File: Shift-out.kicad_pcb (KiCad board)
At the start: 2 copper layers, 116.8 x 33 mm, 23 parts, among them P1 CONN_02X08, P10 CONN_01X08, P11 CONN_01X02, P2 CONN_01X08, P3 CONN_02X08, P4 CONN_01X08, P5 INPUT, P6 CONN_02X08, P7 EXPANSION, P8 CONN_01X08, P9 CONN_02X08, U1 74HC595, U2 74HC595, U3 74HC595, U4 74HC595

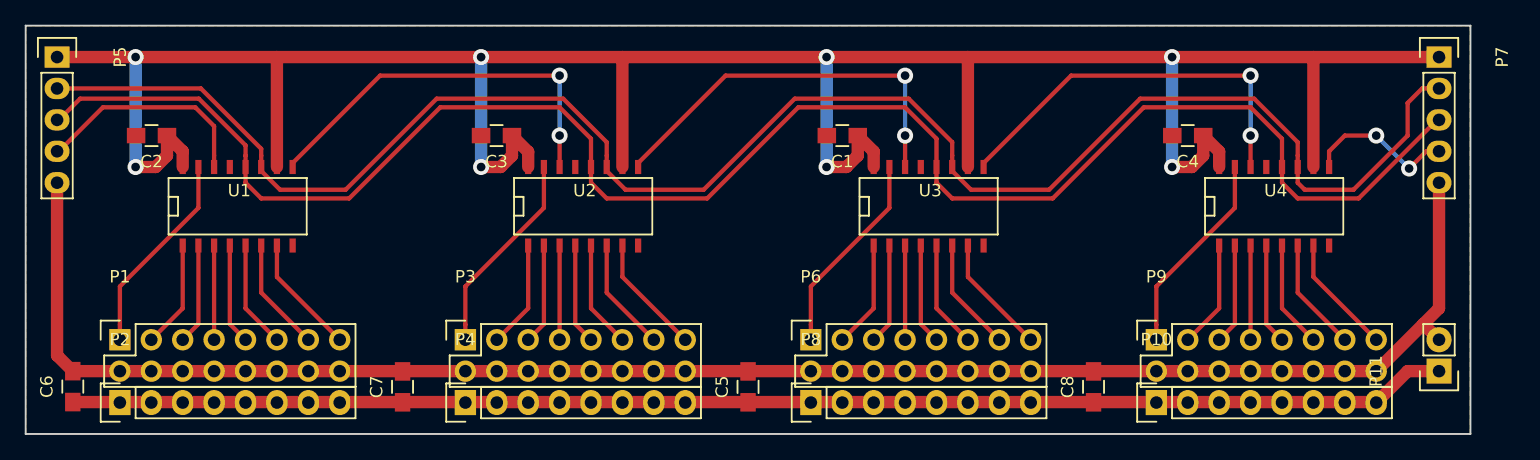
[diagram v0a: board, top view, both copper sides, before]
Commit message: Modified output connector to allow direct servo plugging.
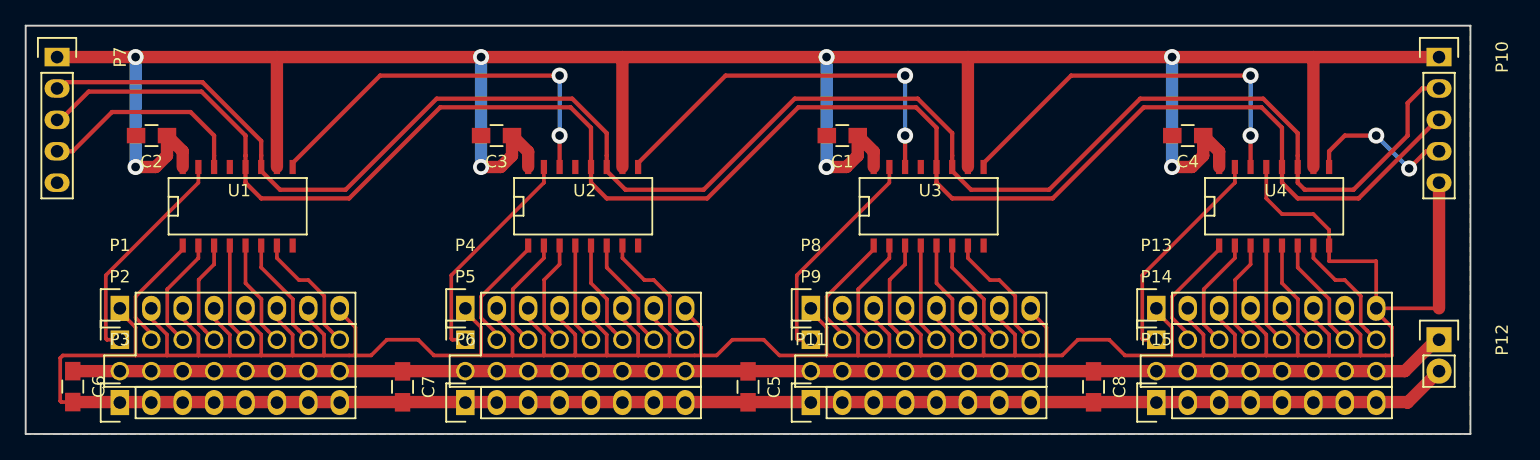
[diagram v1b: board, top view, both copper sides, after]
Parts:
- added P1: CONN_01X08, Socket_Strips:Socket_Strip_Straight_1x08, F.Cu at (106.7, 100.3)
- added P13: CONN_01X08, Socket_Strips:Socket_Strip_Straight_1x08, F.Cu at (190.5, 100.3)
- added P4: CONN_01X08, Socket_Strips:Socket_Strip_Straight_1x08, F.Cu at (134.6, 100.3)
- added P8: CONN_01X08, Socket_Strips:Socket_Strip_Straight_1x08, F.Cu at (162.6, 100.3)
- moved P12 2.54 mm to (213.4, 102.9), turned to 270 degrees
- turned C5 to 270 degrees
- turned C6 to 270 degrees
- turned C7 to 270 degrees
- turned C8 to 270 degrees
- renumbered P7 to P10, P8 to P11, P11 to P12, P9 to P14, P10 to P15, P1 to P2, P2 to P3, P3 to P5, P4 to P6, P5 to P7, P6 to P9
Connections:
- P11 pad 1: VPP -> GND
- P11 pad 2: VPP -> GND
- P11 pad 3: VPP -> GND
- P11 pad 4: VPP -> GND
- P11 pad 5: VPP -> GND
- P11 pad 6: VPP -> GND
- P11 pad 7: VPP -> GND
- P11 pad 8: VPP -> GND
- P14 pad 10: GND -> VPP
- P14 pad 12: GND -> VPP
- P14 pad 14: GND -> VPP
- P14 pad 16: GND -> VPP
- P14 pad 2: GND -> VPP
- P14 pad 4: GND -> VPP
- P14 pad 6: GND -> VPP
- P14 pad 8: GND -> VPP
- P15 pad 1: VPP -> GND
- P15 pad 2: VPP -> GND
- P15 pad 3: VPP -> GND
- P15 pad 4: VPP -> GND
- P15 pad 5: VPP -> GND
- P15 pad 6: VPP -> GND
- P15 pad 7: VPP -> GND
- P15 pad 8: VPP -> GND
- P2 pad 10: GND -> VPP
- P2 pad 12: GND -> VPP
- P2 pad 14: GND -> VPP
- P2 pad 16: GND -> VPP
- P2 pad 2: GND -> VPP
- P2 pad 4: GND -> VPP
- P2 pad 6: GND -> VPP
- P2 pad 8: GND -> VPP
- P3 pad 1: VPP -> GND
- P3 pad 2: VPP -> GND
- P3 pad 3: VPP -> GND
- P3 pad 4: VPP -> GND
- P3 pad 5: VPP -> GND
- P3 pad 6: VPP -> GND
- P3 pad 7: VPP -> GND
- P3 pad 8: VPP -> GND
- P5 pad 10: GND -> VPP
- P5 pad 12: GND -> VPP
- P5 pad 14: GND -> VPP
- P5 pad 16: GND -> VPP
- P5 pad 2: GND -> VPP
- P5 pad 4: GND -> VPP
- P5 pad 6: GND -> VPP
- P5 pad 8: GND -> VPP
- P6 pad 1: VPP -> GND
- P6 pad 2: VPP -> GND
- P6 pad 3: VPP -> GND
- P6 pad 4: VPP -> GND
- P6 pad 5: VPP -> GND
- P6 pad 6: VPP -> GND
- P6 pad 7: VPP -> GND
- P6 pad 8: VPP -> GND
- P9 pad 10: GND -> VPP
- P9 pad 12: GND -> VPP
- P9 pad 14: GND -> VPP
- P9 pad 16: GND -> VPP
- P9 pad 2: GND -> VPP
- P9 pad 4: GND -> VPP
- P9 pad 6: GND -> VPP
- P9 pad 8: GND -> VPP
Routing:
- net GND: track 140.3 -> 399.9 mm
- net /WCK: track 144.8 -> 147.3 mm
- net /BCK: track 144.1 -> 146.2 mm
- net /Q8: track 16.6 -> 18.2 mm
- net /Q24: track 16.6 -> 18.2 mm
- net /Q16: track 16.6 -> 18.2 mm
- net /Q0: track 16.6 -> 18.2 mm
- net /Q9: track 8.67 -> 9.72 mm
- net /Q1: track 8.67 -> 9.72 mm
- net /Q17: track 8.67 -> 9.72 mm
- net /Q25: track 8.67 -> 9.72 mm
- net /Q26: track 8.15 -> 9.18 mm
- net /Q2: track 8.15 -> 9.18 mm
- net /Q3: track 7.62 -> 8.66 mm
- net /Q27: track 7.62 -> 8.66 mm
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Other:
- net class Default: clearance 0.35 -> 0.24; trace_width 0.35 -> 0.3
- net class Power: clearance 0.35 -> 0.24; trace_width 1 -> 0.3
- rule trace_clearance: 0.35 -> 0.24
